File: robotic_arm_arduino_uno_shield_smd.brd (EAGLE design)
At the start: 44.5 x 53.3 mm, 39 parts, among them J1 (ID,OD)=(2.1,5.5)MM

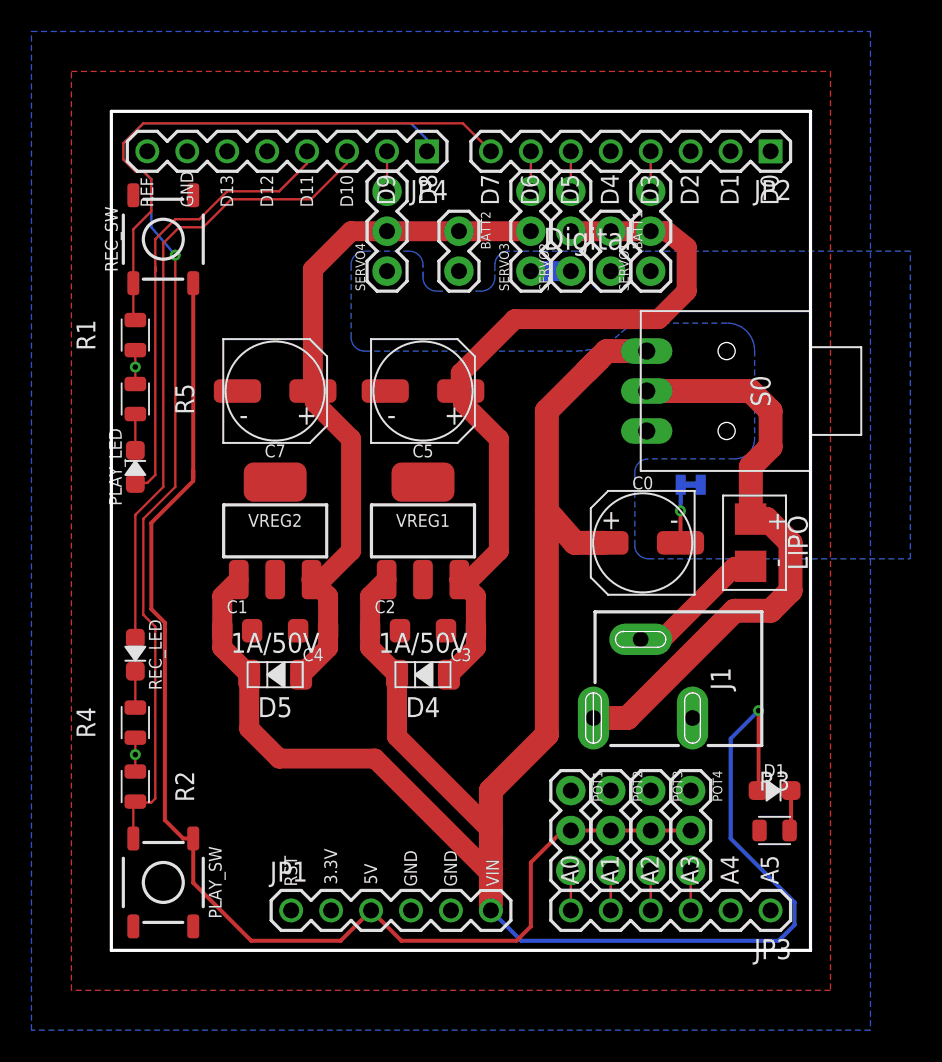
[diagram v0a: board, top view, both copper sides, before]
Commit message: Adjusted some of the traces
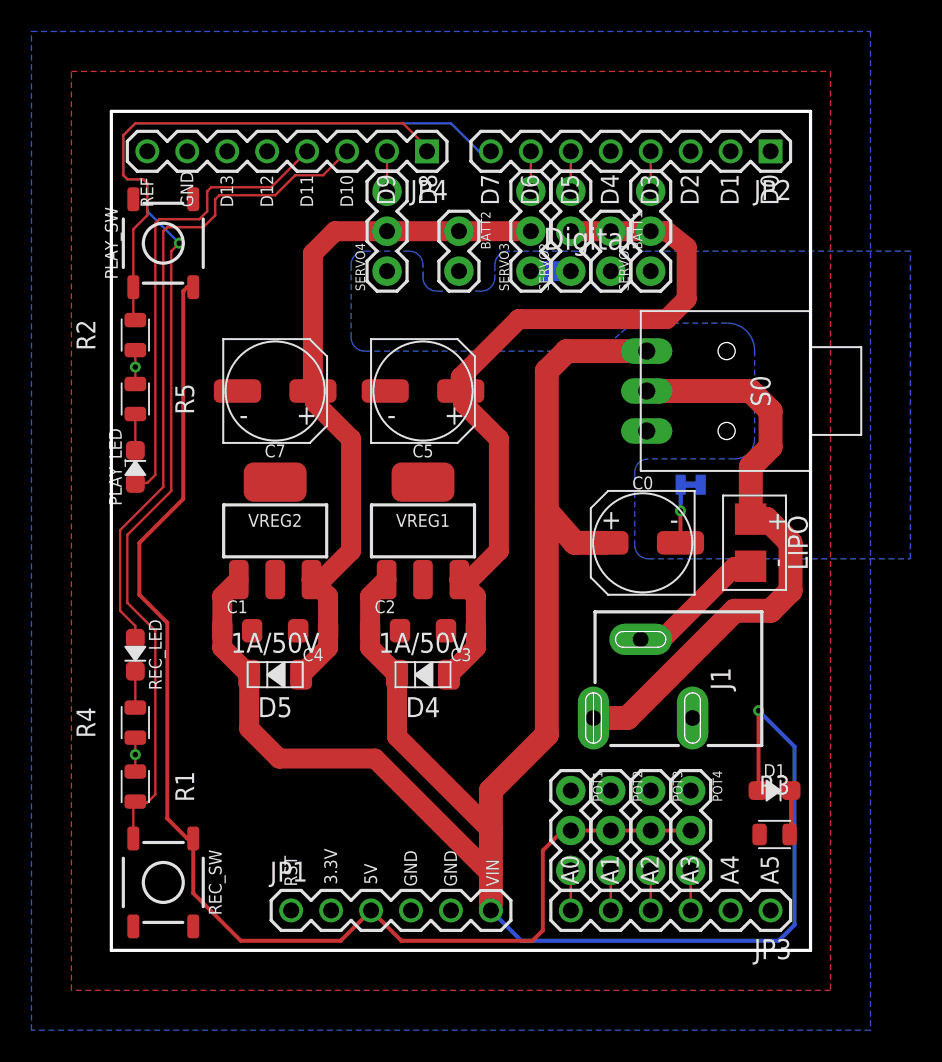
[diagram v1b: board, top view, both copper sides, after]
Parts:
- moved REC_SW 40.9 mm to (3.30, 4.32), turned to 270 degrees
- moved PLAY_SW 40.6 mm to (3.30, 45.0), turned to 90 degrees
- moved R1 28.7 mm to (1.52, 10.4), turned to 270 degrees
- moved R2 28.7 mm to (1.52, 39.1), turned to 90 degrees
- moved R3 0.25 mm to (42.2, 7.37)
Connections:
- net 5V: now also PLAY_SW.3, REC_SW.1; no longer PLAY_SW.1, REC_SW.3
- net D7: now also REC_SW.3; no longer REC_SW.1
- net D8: now also PLAY_SW.1; no longer PLAY_SW.3
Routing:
- net D7: track 37.4 -> 74.4 mm, vias 0 -> 1
- net D8: track 69.2 -> 33.9 mm, vias 1 -> 0
- net D10: track 40.4 -> 41.8 mm
- net VIN: track 137.8 -> 136.7 mm
- net 5V: track 81.4 -> 82.2 mm
- net D11: track 29.1 -> 29.8 mm
- net VCC_2: track 44.2 -> 44.8 mm
